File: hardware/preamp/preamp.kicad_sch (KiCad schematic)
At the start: 20 parts, among them J1 9V DC (centre -), J2 GUITAR IN (6.35 mm), J3 LINE OUT (3.5 mm), U1 OPA1656 (TBD)

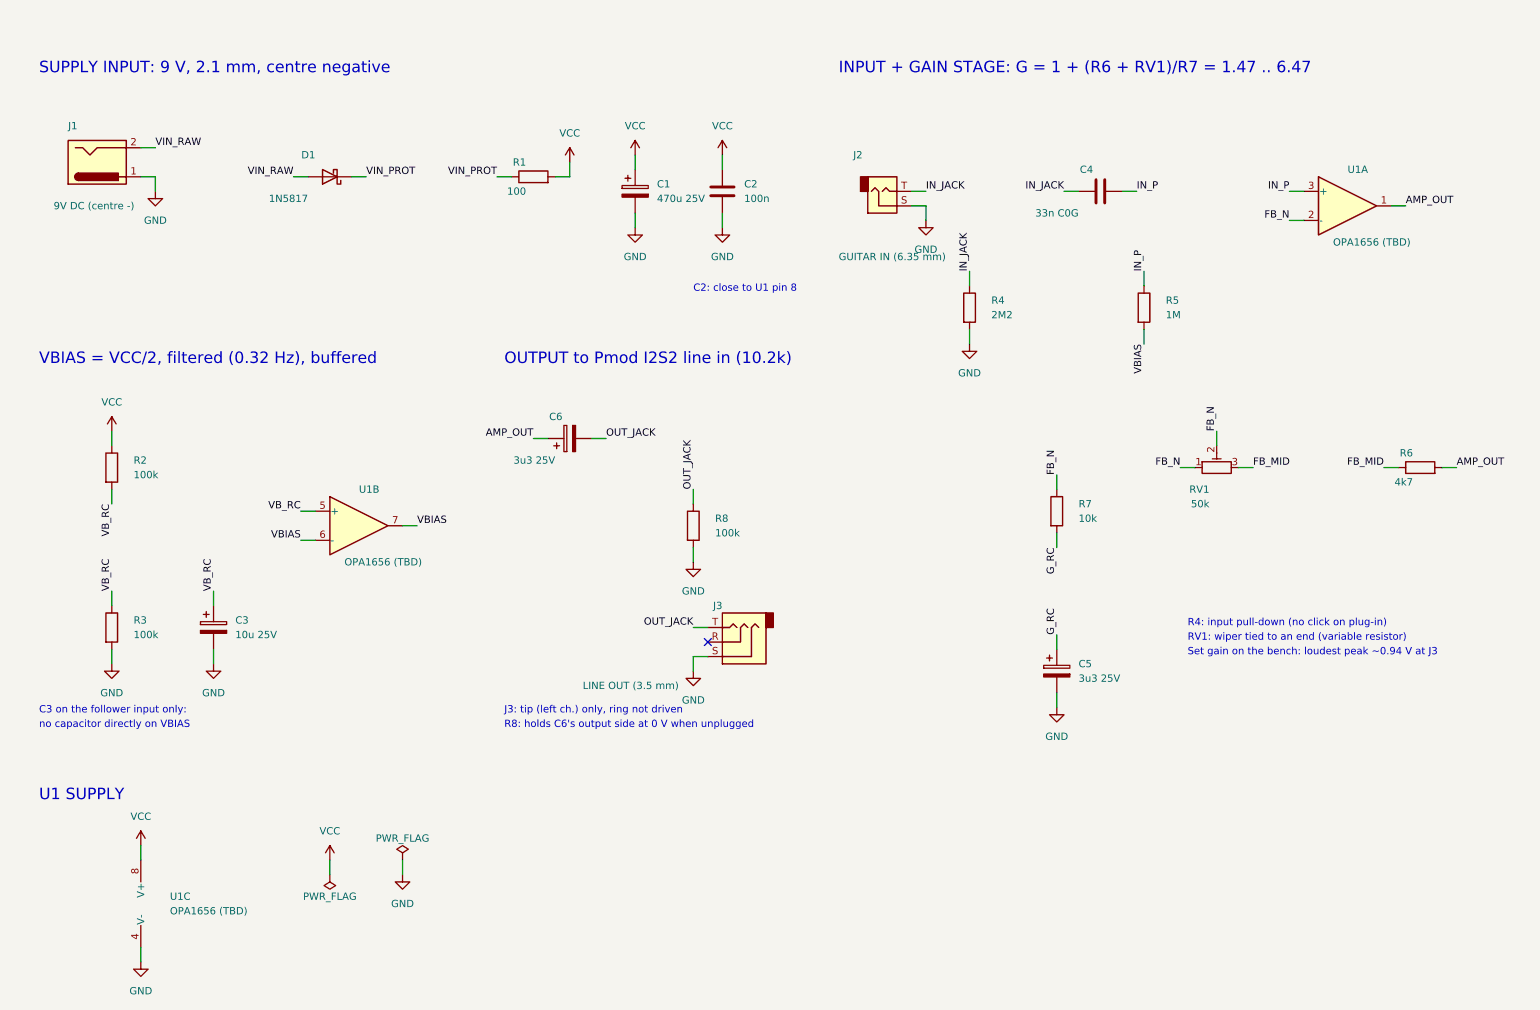
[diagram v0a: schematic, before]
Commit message: Preamp schematic: wiring drawn and tidied (connectivity unchanged)
Netlist checked against the previous commit: every net has the same
pins, no value or footprint changes; only net names differ.

Known ERC: 2 x power_pin_not_driven on +9V_raw and Vin_protect
(power symbols on nets fed only by passive pins; needs PWR_FLAG or
net labels).

.gitignore: KiCad 10 local history (.history/).
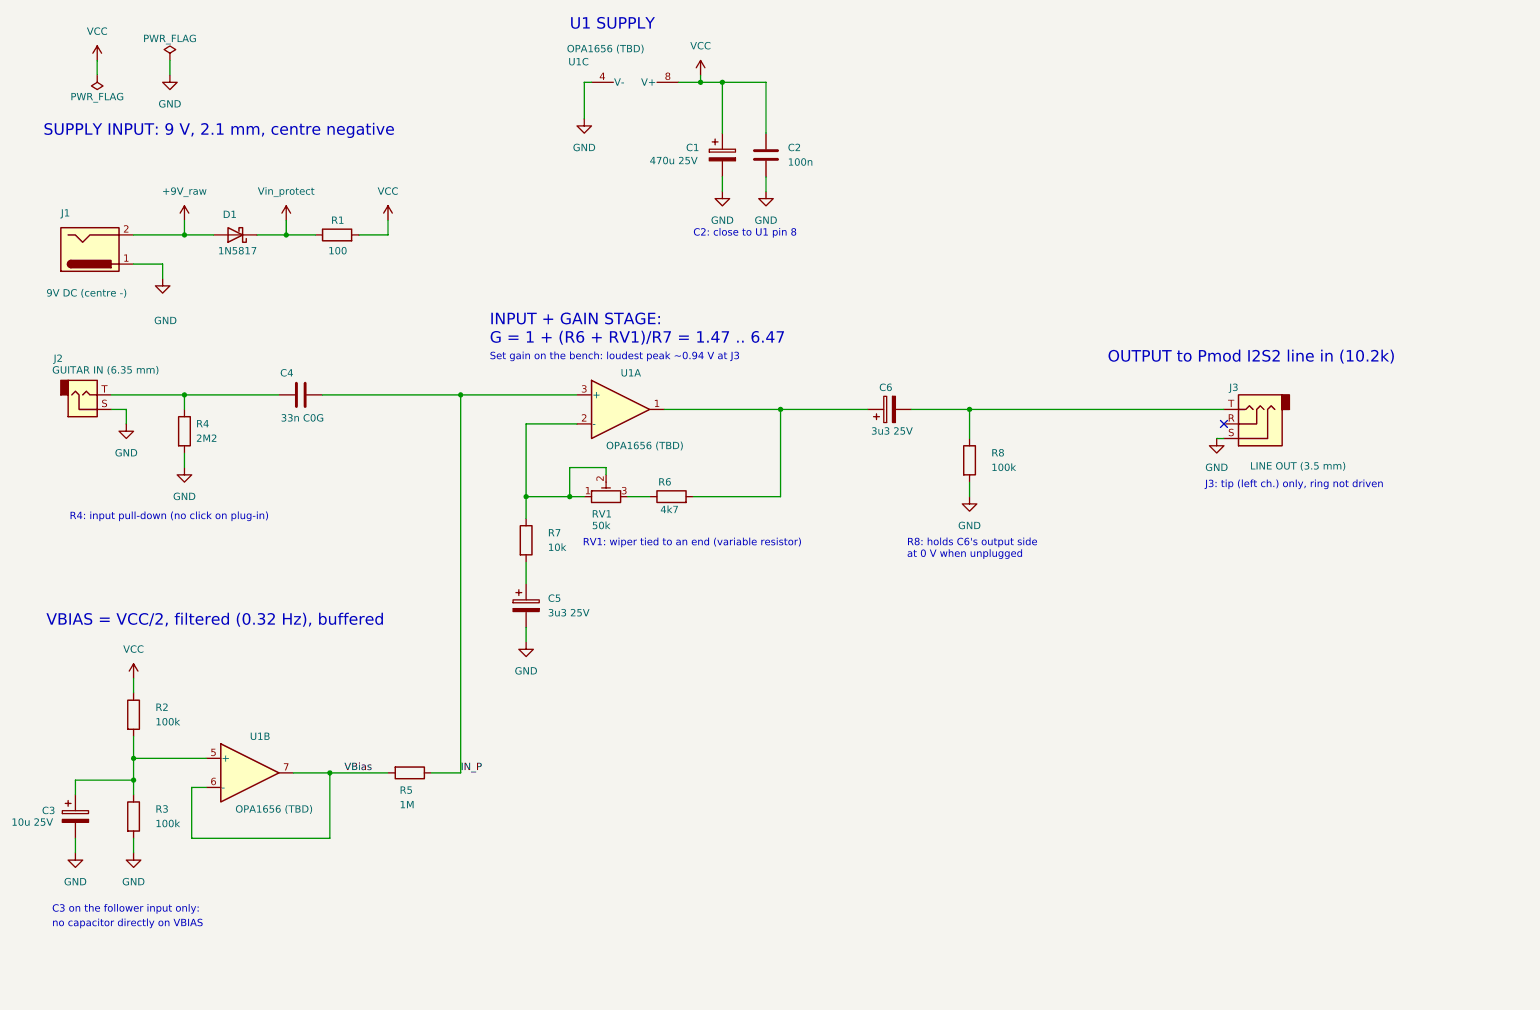
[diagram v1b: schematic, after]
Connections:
- net AMP_OUT: no longer names the net of C6.1, R6.2, U1.1
- net FB_MID: no longer names the net of R6.1, RV1.3
- net FB_N: no longer names the net of R7.1, RV1.1, RV1.2, U1.2 (-)
- net G_RC: no longer names the net of C5.1, R7.2
- net IN_JACK: no longer names the net of C4.1, J2.T, R4.1
- net OUT_JACK: no longer names the net of C6.2, J3.T, R8.1
- net VBIAS renamed VBias
- net VB_RC: no longer names the net of C3.1, R2.2, R3.1, U1.5 (+)
- net VIN_PROT renamed Vin_protect
- net VIN_RAW renamed +9V_raw
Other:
- moved on the sheet: C1, C2, C3, C4, C5, C6, D1, J1, J2, J3, R1, R2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

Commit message: Preamp: C1 470u -> 100u 25V (16 Hz supply filter is enough; VBias has its own); remove the renamed +9V power symbols on +9V_raw / Vin_protect, fixing the two ERC errors
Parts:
- C1: value 470u 25V -> 100u 25V
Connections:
- net +9V_raw: no longer names the net of D1.2 (A), J1.2
- net Vin_protect: no longer names the net of D1.1 (K), R1.1
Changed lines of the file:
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@@
 	)
 	(junction
-		(at 45.72 53.34)
-		(diameter 0)
-		(color 0 0 0 0)
-	)
-	(junction
 		(at 135.89 26.67)
 		(diameter 0)
@@
 	)
 	(junction
-		(at 63.5 53.34)
-		(diameter 0)
-		(color 0 0 0 0)
-	)
-	(junction
 		(at 139.7 26.67)
 		(diameter 0)
@@
 	(wire
 		(pts
-			(xy 36.83 53.34) (xy 45.72 53.34)
-		)
-		(stroke
-			(width 0)
-			(type default)
-		)
-	)
-	(wire
-		(pts
 			(xy 46.99 158.75) (xy 46.99 149.86)
 		)
@@
 	(wire
 		(pts
-			(xy 45.72 53.34) (xy 50.8 53.34)
+			(xy 36.83 53.34) (xy 50.8 53.34)
 		)
 		(stroke
@@
 	(wire
 		(pts
-			(xy 63.5 50.8) (xy 63.5 53.34)
-		)
-		(stroke
-			(width 0)
-			(type default)
-		)
-	)
-	(wire
-		(pts
 			(xy 182.88 96.52) (xy 182.88 99.06)
 		)
@@
 	(wire
 		(pts
-			(xy 45.72 50.8) (xy 45.72 53.34)
-		)
-		(stroke
-			(width 0)
-			(type default)
-		)
-	)
-	(wire
-		(pts
 			(xy 33.02 83.82) (xy 35.56 83.82)
 		)
@@
 	(wire
 		(pts
-			(xy 63.5 53.34) (xy 68.58 53.34)
+			(xy 58.42 53.34) (xy 68.58 53.34)
 		)
 		(stroke
@@
 	(wire
 		(pts
-			(xy 58.42 53.34) (xy 63.5 53.34)
-		)
-		(stroke
-			(width 0)
-			(type default)
-		)
-	)
-	(wire
-		(pts
 			(xy 71.12 147.32) (xy 81.28 147.32)
 		)
@@
 	)
 	(symbol
-		(lib_id "power:+9V")
-		(at 45.72 50.8 0)
-		(unit 1)
-		(body_style 1)
-		(exclude_from_sim no)
-		(in_bom yes)
-		(on_board yes)
-		(in_pos_files yes)
-		(dnp no)
-		(fields_autoplaced yes)
-		(property "Reference" "#PWR019"
-			(at 45.72 54.61 0)
-			(hide yes)
-			(show_name no)
-			(do_not_autoplace no)
-			(effects
-				(font
-					(size 1.27 1.27)
-				)
-			)
-		)
-		(property "Value" "+9V_raw"
-			(at 45.72 45.72 0)
-			(show_name no)
-			(do_not_autoplace no)
-			(effects
-				(font
-					(size 1.27 1.27)
-				)
-			)
-		)
-		(property "Footprint" ""
-			(at 45.72 50.8 0)
-			(hide yes)
-			(show_name no)
-			(do_not_autoplace no)
-			(effects
-				(font
-					(size 1.27 1.27)
-				)
-			)
-		)
-		(property "Datasheet" ""
-			(at 45.72 50.8 0)
-			(hide yes)
-			(show_name no)
-			(do_not_autoplace no)
-			(effects
-				(font
-					(size 1.27 1.27)
-				)
-			)
-		)
-		(property "Description" "Power symbol creates a global label with name \"+9V\""
-			(at 45.72 50.8 0)
-			(hide yes)
-			(show_name no)
-			(do_not_autoplace no)
-			(effects
-				(font
-					(size 1.27 1.27)
-				)
-			)
-		)
-		(pin "1"
-		)
-		(instances
-			(project "preamp"
-				(path "/b570cdde-1936-5608-96c2-4a74dd01f7d2"
-					(reference "#PWR019")
-					(unit 1)
-				)
-			)
-		)
-	)
-	(symbol
 		(lib_id "Device:R")
 		(at 130.81 99.06 90)
@@
 	)
 	(symbol
-		(lib_id "power:+9V")
-		(at 63.5 50.8 0)
-		(unit 1)
-		(body_style 1)
-		(exclude_from_sim no)
-		(in_bom yes)
-		(on_board yes)
-		(in_pos_files yes)
-		(dnp no)
-		(fields_autoplaced yes)
-		(property "Reference" "#PWR020"
-			(at 63.5 54.61 0)
-			(hide yes)
-			(show_name no)
-			(do_not_autoplace no)
-			(effects
-				(font
-					(size 1.27 1.27)
-				)
-			)
-		)
-		(property "Value" "Vin_protect"
-			(at 63.5 45.72 0)
-			(show_name no)
-			(do_not_autoplace no)
-			(effects
-				(font
-					(size 1.27 1.27)
-				)
-			)
-		)
-		(property "Footprint" ""
-			(at 63.5 50.8 0)
-			(hide yes)
-			(show_name no)
-			(do_not_autoplace no)
-			(effects
-				(font
-					(size 1.27 1.27)
-				)
-			)
-		)
-		(property "Datasheet" ""
-			(at 63.5 50.8 0)
-			(hide yes)
-			(show_name no)
-			(do_not_autoplace no)
-			(effects
-				(font
-					(size 1.27 1.27)
-				)
-			)
-		)
-		(property "Description" "Power symbol creates a global label with name \"+9V\""
-			(at 63.5 50.8 0)
-			(hide yes)
-			(show_name no)
-			(do_not_autoplace no)
-			(effects
-				(font
-					(size 1.27 1.27)
-				)
-			)
-		)
-		(pin "1"
-		)
-		(instances
-			(project "preamp"
-				(path "/b570cdde-1936-5608-96c2-4a74dd01f7d2"
-					(reference "#PWR020")
-					(unit 1)
-				)
-			)
-		)
-	)
-	(symbol
 		(lib_id "Device:C_Polarized")
 		(at 105.41 118.11 0)
@@
 			)
 		)
-		(property "Value" "470u 25V"
+		(property "Value" "100u 25V"
 			(at 127 40.386 0)
 			(show_name no)

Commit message: Preamp: footprints for every part (prototype, PCB-mount jacks): SMD electrolytics, Bourns 3296W trimmer, D1 1N5817 -> SS14 (SMA), CUI PJ-102AH / Neutrik NMJ4HCD2 / CUI SJ1-3523N jacks
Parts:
- C1: footprint (none) -> Capacitor_SMD:CP_Elec_6.3x7.7
- C3, C5, C6: footprint (none) -> Capacitor_SMD:CP_Elec_4x5.4
- D1: value 1N5817 -> SS14; footprint Diode_THT:D_DO-41_SOD81_P10.16mm_Horizontal -> Diode_SMD:D_SMA_Handsoldering; symbol Diode:1N5817 -> Diode:SS14
- J1: footprint (none) -> Connector_BarrelJack:BarrelJack_CUI_PJ-102AH_Horizontal
- J2: footprint (none) -> Connector_Audio:Jack_6.35mm_Neutrik_NMJ4HCD2_Horizontal
- J3: footprint (none) -> Connector_Audio:Jack_3.5mm_CUI_SJ1-3523N_Horizontal
- RV1: footprint (none) -> Potentiometer_THT:Potentiometer_Bourns_3296W_Vertical
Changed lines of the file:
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@@
 			)
 		)
-		(property "Footprint" ""
+		(property "Footprint" "Capacitor_SMD:CP_Elec_4x5.4"
 			(at 168.91 83.82 0)
 			(hide yes)
@@
 			)
 		)
-		(property "Footprint" ""
+		(property "Footprint" "Potentiometer_THT:Potentiometer_Bourns_3296W_Vertical"
 			(at 119.38 99.06 0)
 			(hide yes)
@@
 			)
 		)
-		(property "Footprint" ""
+		(property "Footprint" "Connector_BarrelJack:BarrelJack_CUI_PJ-102AH_Horizontal"
 			(at 29.21 55.88 0)
 			(hide yes)
@@
 			)
 		)
-		(property "Footprint" ""
+		(property "Footprint" "Connector_Audio:Jack_3.5mm_CUI_SJ1-3523N_Horizontal"
 			(at 232.41 86.36 0)
 			(hide yes)
@@
 			)
 		)
-		(property "Footprint" ""
+		(property "Footprint" "Connector_Audio:Jack_6.35mm_Neutrik_NMJ4HCD2_Horizontal"
 			(at 27.94 81.28 0)
 			(hide yes)
@@
 			)
 		)
-		(property "Footprint" ""
+		(property "Footprint" "Capacitor_SMD:CP_Elec_4x5.4"
 			(at 26.67 154.94 0)
 			(hide yes)
@@
 	)
 	(symbol
-		(lib_id "Diode:1N5817")
+		(lib_id "Diode:SS14")
 		(at 54.61 53.34 180)
 		(unit 1)
@@
 			)
 		)
-		(property "Value" "1N5817"
+		(property "Value" "SS14"
 			(at 58.42 56.134 0)
 			(show_name no)
@@
 			)
 		)
-		(property "Footprint" "Diode_THT:D_DO-41_SOD81_P10.16mm_Horizontal"
+		(property "Footprint" "Diode_SMD:D_SMA_Handsoldering"
 			(at 54.61 53.34 0)
 			(hide yes)
@@
 			)
 		)
-		(property "Datasheet" "http://www.vishay.com/docs/88525/1n5817.pdf"
+		(property "Datasheet" "https://www.vishay.com/docs/88746/ss12.pdf"
 			(at 54.61 53.34 0)
 			(hide yes)
@@
 			)
 		)
-		(property "Description" "20V 1A Schottky Barrier Rectifier Diode, DO-41"
+		(property "Description" "40V 1A Schottky Diode, SMA"
 			(at 54.61 53.34 0)
 			(hide yes)
@@
 			)
 		)
-		(property "Footprint" ""
+		(property "Footprint" "Capacitor_SMD:CP_Elec_4x5.4"
 			(at 105.41 118.11 0)
 			(hide yes)
@@
 			)
 		)
-		(property "Footprint" ""
+		(property "Footprint" "Capacitor_SMD:CP_Elec_6.3x7.7"
 			(at 139.7 39.37 0)
 			(hide yes)

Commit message: Preamp: op-amp chosen, U1 = OPA1642AID (OPA1656ID symbol, same dual SOIC-8 pinout); doc lists why and the drop-in alternatives
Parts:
- U1: value OPA1656 (TBD) -> OPA1642AID
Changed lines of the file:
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@@
 			)
 		)
-		(property "Value" "OPA1656 (TBD)"
+		(property "Value" "OPA1642AID"
 			(at 112.522 20.828 90)
 			(show_name no)
@@
 			)
 		)
-		(property "Value" "OPA1656 (TBD)"
+		(property "Value" "OPA1642AID"
 			(at 54.61 153.67 0)
 			(show_name no)
@@
 			)
 		)
-		(property "Value" "OPA1656 (TBD)"
+		(property "Value" "OPA1642AID"
 			(at 119.38 90.17 0)
 			(show_name no)
